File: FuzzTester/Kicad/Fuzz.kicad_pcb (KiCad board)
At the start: 2 copper layers, 180 x 100 mm, 133 parts, among them J1 Audio In/Out JST XH, J10 Key Pad JST XH, J11 1602 LCD JST XH, J2 POT B10K JST XH, J3 POT B5K JST XH, J4 VOL POT A100K JST XH, J5 TestPower_PinHeader, J6 9V Power JST XH, J7 Boot Reset PinHeader, J8 SPI Test PinHeader, J9 SWD_PinHeader, Q1 PN2222A, Q10 2SC1815, Q11 S8050, Q12 S9013, Q13 S9014, Q14 S9018, Q15 BC848B, Q16 2SC1623, Q17 MPSA18, Q18 MPSA18, Q19 2N5088, Q2 MMBT3904, Q20 2N5088, Q21 PN2222A, Q22 MMBT3904, Q23 MMBT5551L, Q24 MMBTA42, Q25 BC807, Q26 BC846, Q27 BC847B, Q28 BC847C, Q29 C945, Q3 MMBT5551L, Q30 2SC1815, Q31 S8050, Q32 S9013, Q33 S9014, Q34 S9018, Q35 BC848B, Q36 2SC1623, Q37 MPSA18, Q38 MPSA18, Q39 2N5088, Q4 MMBTA42, Q40 2N5088, Q5 BC807, Q6 BC846, Q7 BC847B, Q8 BC847C, Q9 C945, U1 AMS1117-5.0, U10 CD4052B, U11 CD4052B, U12 CD4052B, U13 CD4052B, U14 CD4051B, U15 CD4052B, U16 CD4051B, U17 CD4052B, U18 CD4052B, U19 CD4052B, U2 AMS1117-3.3, U20 74HC595, U21 CD4051B, U3 STM32F103C8Tx, U4 CD4051B, U5 74HC595, U6 CD4052B, U7 CD4051B, U8 CD4052B, U9 CD4051B, Y1 8MHz

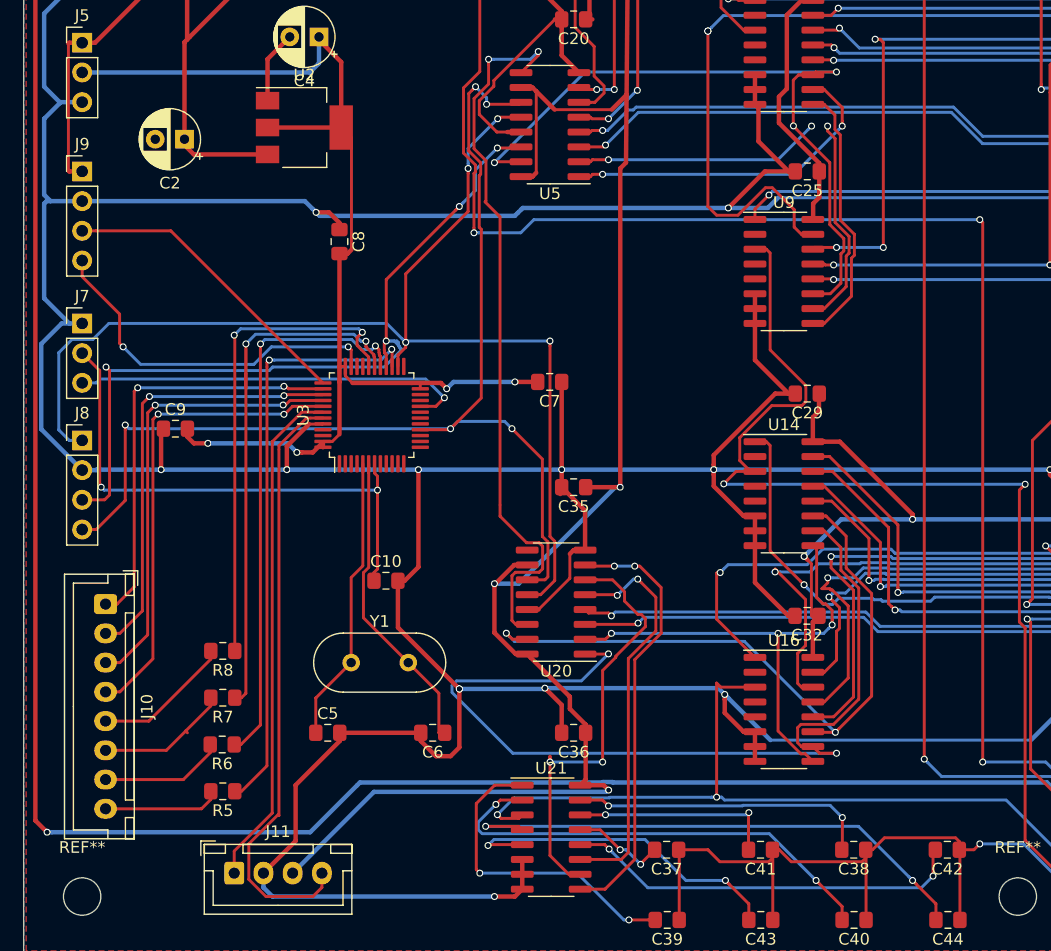
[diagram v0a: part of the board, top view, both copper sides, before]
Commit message: Improved PCB SPI/I2C lines
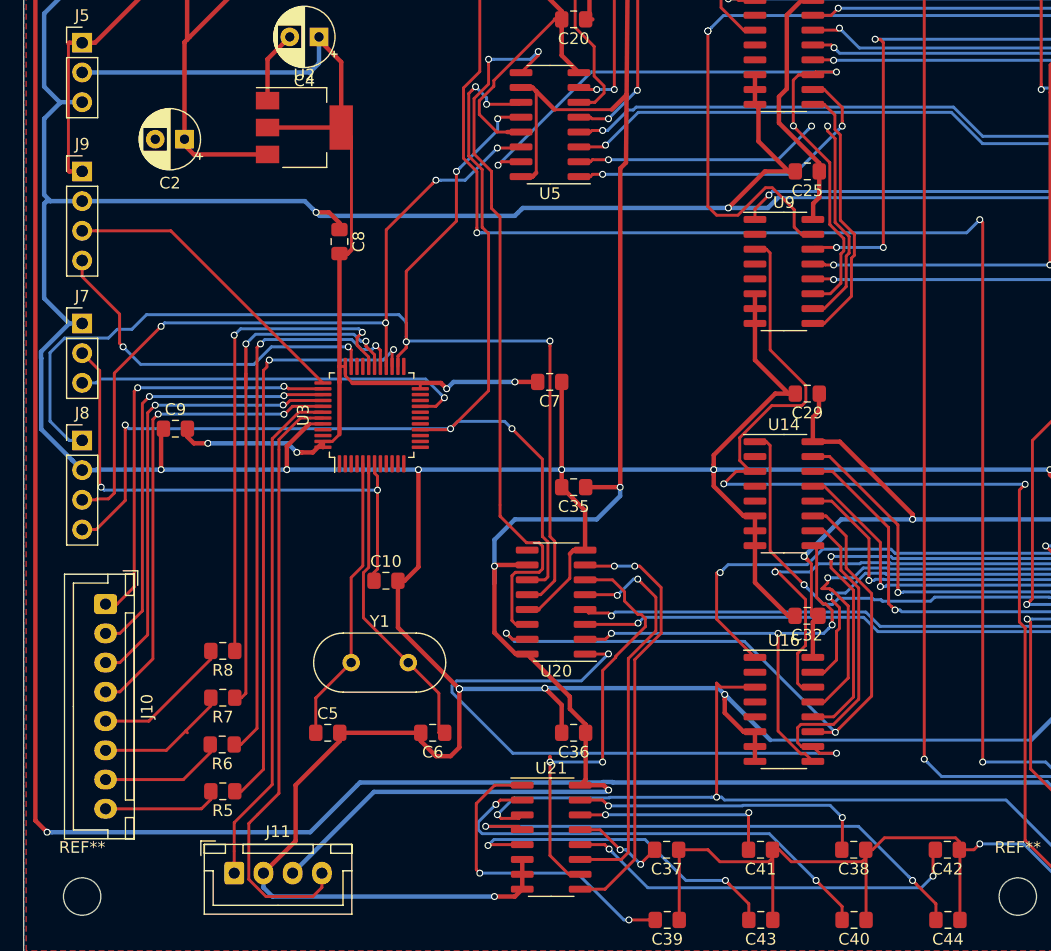
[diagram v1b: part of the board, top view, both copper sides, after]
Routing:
- net /SPI2_MOSI: track 68.0 -> 64.4 mm
- net +5V: track 573.1 -> 576.7 mm
- net /SPI2_CSK: track 103.0 -> 105.6 mm
- net GND: track 1307.9 -> 1307.1 mm

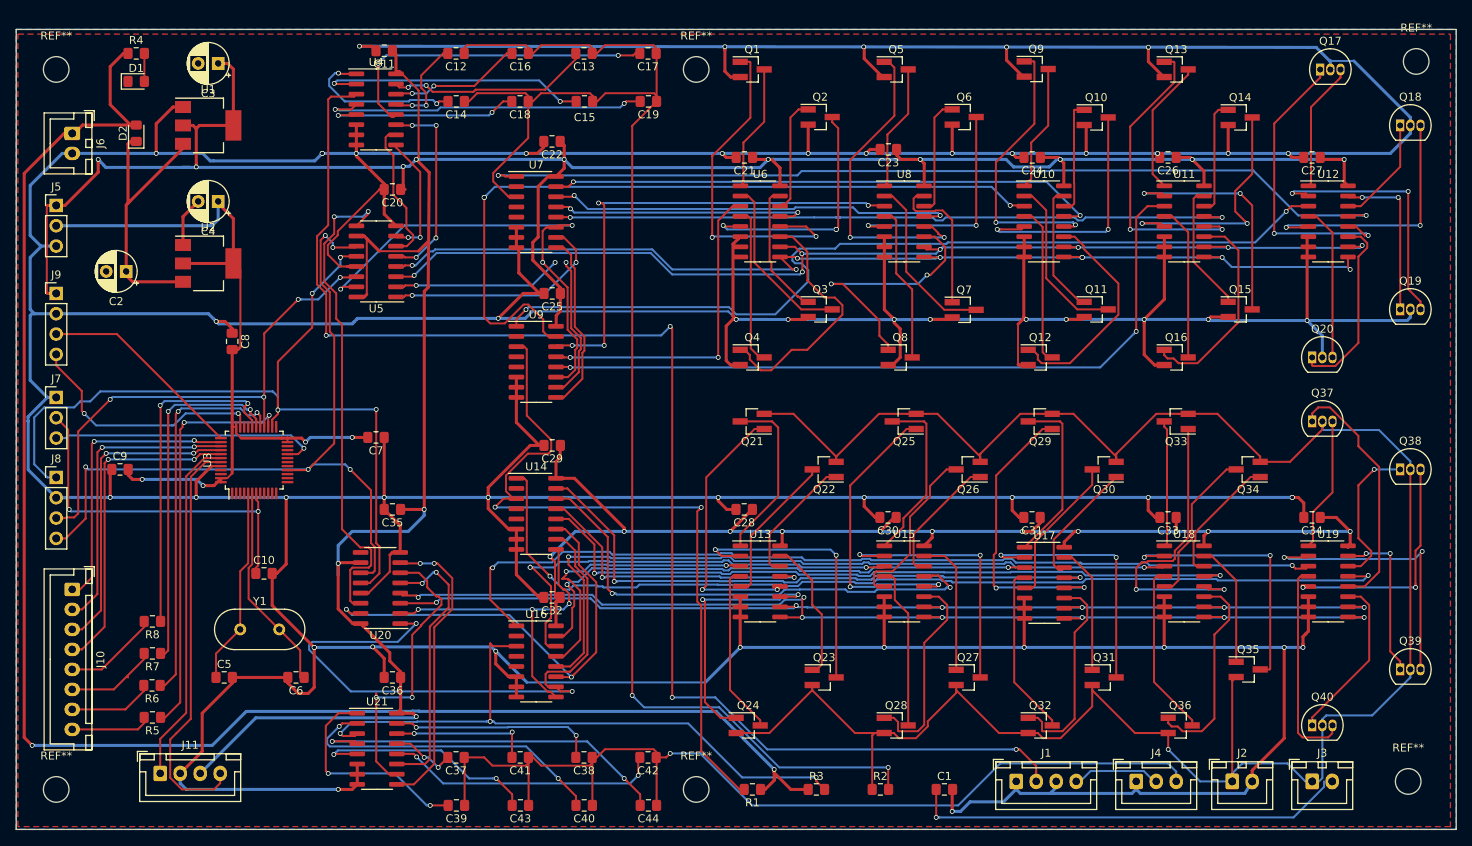
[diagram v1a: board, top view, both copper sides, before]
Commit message: Fixed unconnected PCB traces
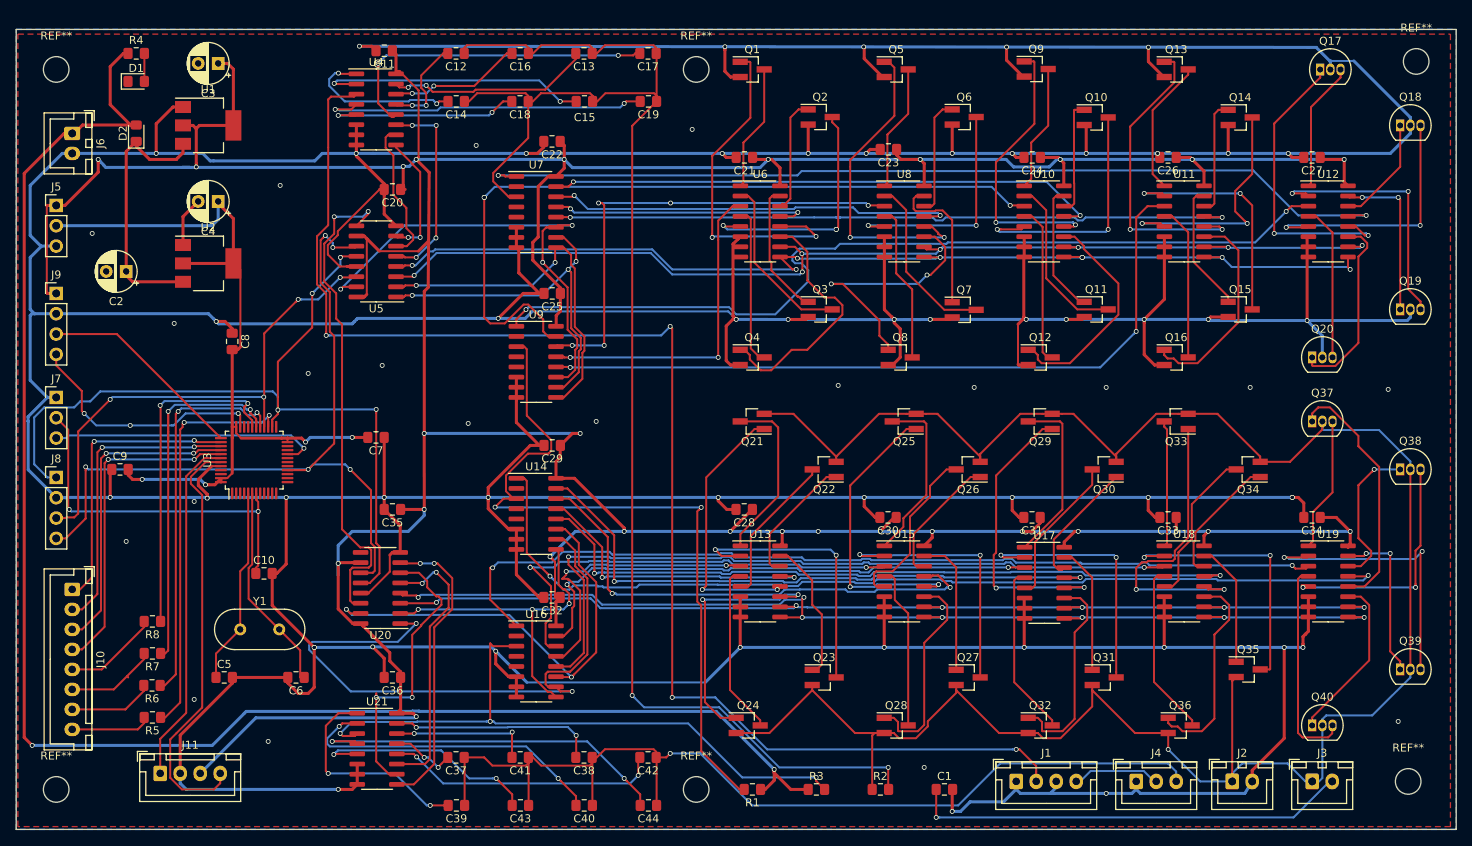
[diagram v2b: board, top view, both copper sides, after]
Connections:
- C2 pad 1: +9V -> Net-(C2-Pad1)
- D2 pad 1: +9V -> Net-(C2-Pad1)
- U1 pad 3: +9V -> Net-(C2-Pad1)
- U2 pad 3: +9V -> Net-(C2-Pad1)
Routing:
- net +9V: track 242.7 -> 207.4 mm
- net Net-(C2-Pad1): track 0.00 -> 33.3 mm
- net +5V: track 576.7 -> 599.9 mm, vias 24 -> 27
- net /TRANSISTOR_B_GROUP_SELECTION_2: track 44.0 -> 45.9 mm
- net /TRANSISTOR_B_GROUP_SELECTION_1: track 47.4 -> 46.2 mm
- net /Mcu/I2C1_SDA: track 51.6 -> 52.8 mm
- net Net-(C1-Pad1): track 54.2 -> 54.9 mm
- net GND: track 1307.1 -> 1307.6 mm, vias 53 -> 72
- net /TransistorsB/TG_2_COLLECTOR: vias 4 -> 5
- net /Mcu/SYS_JTMS_SWDIO: vias 2 -> 3

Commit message: Schematics UI/MCU -> MCU + PCB improvements
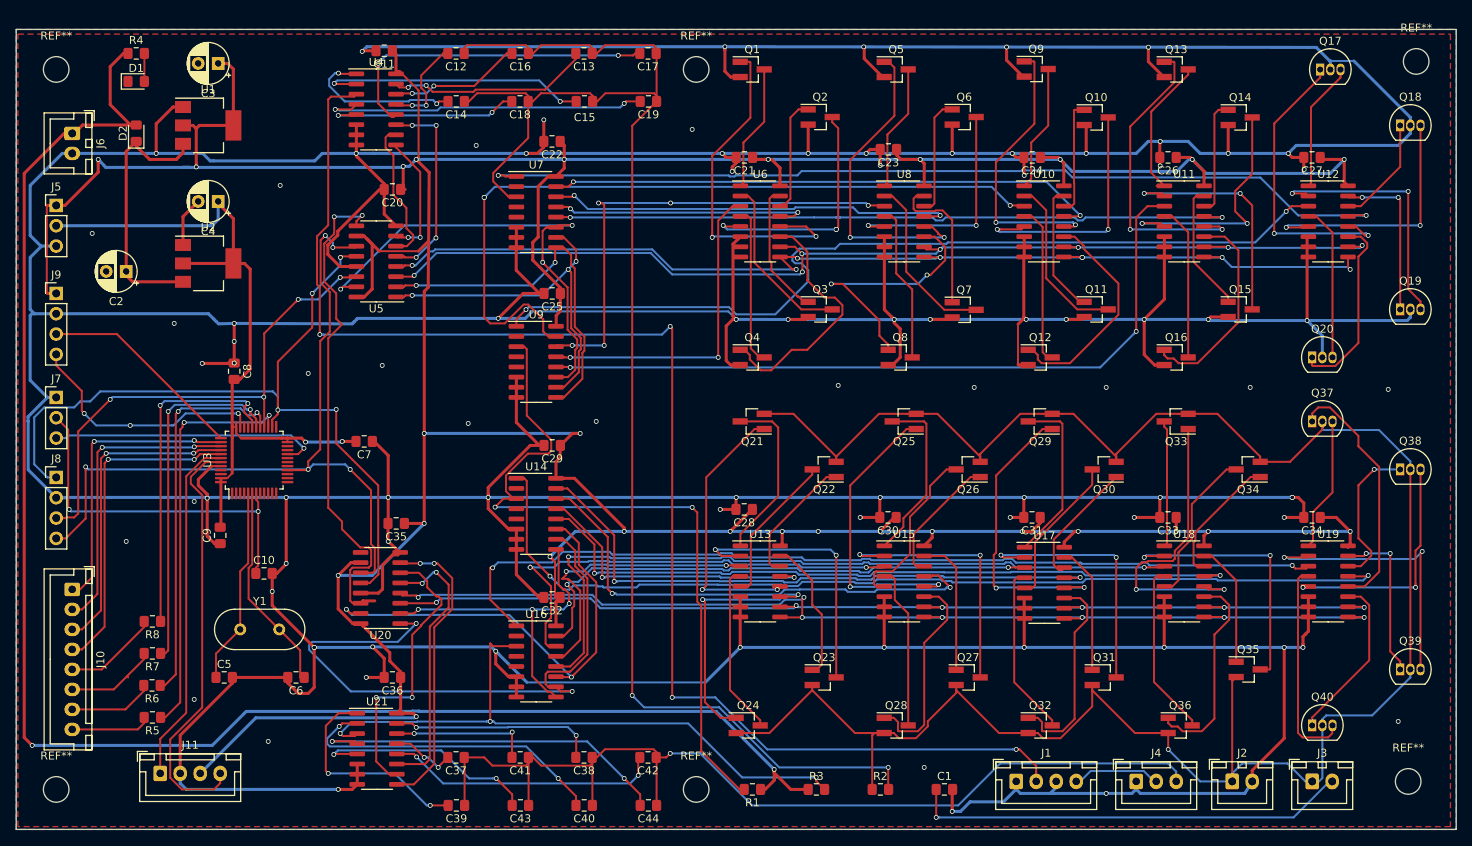
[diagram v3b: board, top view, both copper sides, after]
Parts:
- moved C9 15.0 mm to (54.5, 84.2), turned to 90 degrees
- moved C8 3.73 mm to (56.2, 63.7)
- moved C35 1.81 mm to (76.5, 82.8)
- moved C7 1.56 mm to (72.5, 72.5)
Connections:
- R5 pad 2: Net-(J10-Pad8) -> Net-(R5-Pad2)
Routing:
- net GND: track 1307.6 -> 1339.9 mm, vias 72 -> 89
- net +3V3: track 98.4 -> 92.2 mm, vias 4 -> 2
- net /SPI2_CSK: track 105.6 -> 102.5 mm
- net /ShiftRegistersCD/COMPONENT_SELECTION_INPUT: track 62.1 -> 63.7 mm
- net +5V: track 599.9 -> 598.5 mm
- net /TransistorsB/13_COLLECTOR: track 17.0 -> 18.1 mm
- net /TransistorsC/BASE: track 93.2 -> 92.1 mm
- net /CAPACITOR_D_SELECTION_1: track 37.5 -> 36.5 mm

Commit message: PCB Placement 100x82
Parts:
- removed REF** (x6): MountingHole_3.2mm_M3, MountingHole:MountingHole_3.2mm_M3
- added C45: 100nF, Capacitor_SMD:C_0805_2012Metric_Pad1.15x1.40mm_HandSolder, B.Cu at (63.3, 32.3)
- added C46: 100nF, Capacitor_SMD:C_0805_2012Metric_Pad1.15x1.40mm_HandSolder, B.Cu at (63.0, 98.5)
- added C47: 100nF, Capacitor_SMD:C_0805_2012Metric_Pad1.15x1.40mm_HandSolder, B.Cu at (62.5, 46.0)
- added C48: 100nF, Capacitor_SMD:C_0805_2012Metric_Pad1.15x1.40mm_HandSolder, B.Cu at (63.1, 86.4)
- added H1: MountingHole, MountingHole:MountingHole_3.2mm_M3, F.Cu at (126.5, 33.5)
- added H2: MountingHole, MountingHole:MountingHole_3.2mm_M3, F.Cu at (126.5, 108.5)
- added H3: MountingHole, MountingHole:MountingHole_3.2mm_M3, F.Cu at (33.5, 108.5)
- added H4: MountingHole, MountingHole:MountingHole_3.2mm_M3, F.Cu at (33.5, 33.5)
- added J12: Bypass Switch JST XH, Connector_JST:JST_XH_B2B-XH-A_1x02_P2.50mm_Vertical, F.Cu at (45.2, 99.1)
- added U22: 4504, Package_SO:SOIC-16_3.9x9.9mm_P1.27mm, F.Cu at (61.0, 52.0)
- added U23: 4504, Package_SO:SOIC-16_3.9x9.9mm_P1.27mm, F.Cu at (61.7, 92.9)
- added U24: 4504, Package_SO:SOIC-16_3.9x9.9mm_P1.27mm, F.Cu at (61.8, 105.1)
- added U25: CD4053B, Package_SO:SOIC-16_3.9x9.9mm_P1.27mm, F.Cu at (61.2, 38.5)
- C1: footprint Capacitor_SMD:C_0805_2012Metric_Pad1.15x1.40mm_HandSolder -> Capacitor_THT:CP_Radial_D5.0mm_P2.50mm
- C10, C11, C20, C21, C22, C23, C24, C25, C26, C27, C28, C29, C30, C31, C32, C33, C34, C35, C36, C5, C6, C7, C8, C9: moved to B.Cu
- J11: value 1602 LCD JST XH -> LCD JST XH; footprint Connector_JST:JST_XH_B4B-XH-A_1x04_P2.50mm_Vertical -> Connector_JST:JST_XH_B6B-XH-A_1x06_P2.50mm_Vertical
- J5: value TestPower_PinHeader -> PowerTest_PinHeader; footprint Connector_PinHeader_2.54mm:PinHeader_1x03_P2.54mm_Vertical -> Connector_PinHeader_2.54mm:PinHeader_1x04_P2.54mm_Vertical
- R1, R2, R3: footprint Resistor_SMD:R_0805_2012Metric_Pad1.15x1.40mm_HandSolder -> Resistor_SMD:R_1206_3216Metric_Pad1.42x1.75mm_HandSolder
- moved J3 109.1 mm to (117.3, 34.5)
- moved J2 108.3 mm to (108.5, 34.5)
- moved J4 107.8 mm to (97.2, 34.5)
- moved J1 107.1 mm to (83.3, 34.5)
- moved C1 103.3 mm to (75.0, 40.0)
- moved Q9 103.2 mm to (84.0, 99.4)
- moved R2 102.2 mm to (69.2, 39.6)
- moved Q10 102.0 mm to (84.0, 95.2)
- moved R3 97.3 mm to (76.7, 34.0)
- moved R1 96.8 mm to (69.1, 34.3)
- moved Q6 86.9 mm to (83.9, 91.1)
- moved Q18 83.7 mm to (118.7, 41.5)
- moved Q39 77.5 mm to (125.3, 89.9)
- moved Q5 77.5 mm to (112.3, 98.8)
- moved Q38 76.9 mm to (125.2, 72.4)
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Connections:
- C11 pad 1: +5V -> +9V
- C20 pad 1: +5V -> +3V3
- C21 pad 1: +5V -> +9V
- C22 pad 1: +5V -> +9V
- C23 pad 1: +5V -> +9V
- C24 pad 1: +5V -> +9V
- C25 pad 1: +5V -> +9V
- C26 pad 1: +5V -> +9V
- C27 pad 1: +5V -> +9V
- C28 pad 1: +5V -> +9V
- C29 pad 1: +5V -> +9V
- C30 pad 1: +5V -> +9V
- C31 pad 1: +5V -> +9V
- C32 pad 1: +5V -> +9V
- C33 pad 1: +5V -> +9V
- C34 pad 1: +5V -> +9V
- C35 pad 1: +5V -> +3V3
- C36 pad 1: +5V -> +9V
- J1 pad 2: /JACK_IN_SIGNAL -> /AudioInOut/JACK_IN_SIGNAL
- J1 pad 4: /JACK_OUT_SIGNAL -> /AudioInOut/JACK_OUT_SIGNAL
- J10 pad 1: /Mcu/GPIO_KEYPAD_ROW_1 -> Net-(J10-Pad1)
- J10 pad 2: /Mcu/GPIO_KEYPAD_ROW_2 -> Net-(J10-Pad2)
- J10 pad 3: /Mcu/GPIO_KEYPAD_ROW_3 -> Net-(J10-Pad3)
- J10 pad 4: /Mcu/GPIO_KEYPAD_ROW_4 -> Net-(J10-Pad4)
- J10 pad 5: Net-(J10-Pad5) -> /Mcu/GPIO_KEYPAD_ROW_4
- J10 pad 6: Net-(J10-Pad6) -> /Mcu/GPIO_KEYPAD_ROW_3
- J10 pad 7: Net-(J10-Pad7) -> /Mcu/GPIO_KEYPAD_ROW_2
- J10 pad 8: Net-(J10-Pad8) -> /Mcu/GPIO_KEYPAD_ROW_1
- J4 pad 2: /JACK_OUT_SIGNAL -> /JACK_OUT_SIGNAL_FROM_FUZZ
- J5 pad 1: +5V -> +9V
- J5 pad 2: +3V3 -> +5V
- J5 pad 3: GND -> +3V3
- J6 pad 1: +9V -> GND
- J6 pad 2: GND -> +9V
- R5 pad 1: /Mcu/GPIO_KEYPAD_COLUMN_4 -> /Mcu/GPIO_KEYPAD_COLUMN_1
- R5 pad 2: Net-(R5-Pad2) -> Net-(J10-Pad1)
- R6 pad 1: /Mcu/GPIO_KEYPAD_COLUMN_3 -> /Mcu/GPIO_KEYPAD_COLUMN_2
- R6 pad 2: Net-(J10-Pad7) -> Net-(J10-Pad2)
- R7 pad 1: /Mcu/GPIO_KEYPAD_COLUMN_2 -> /Mcu/GPIO_KEYPAD_COLUMN_3
- R7 pad 2: Net-(J10-Pad6) -> Net-(J10-Pad3)
- R8 pad 1: /Mcu/GPIO_KEYPAD_COLUMN_1 -> /Mcu/GPIO_KEYPAD_COLUMN_4
- R8 pad 2: Net-(J10-Pad5) -> Net-(J10-Pad4)
- U10 pad 16: +5V -> +9V
- U11 pad 16: +5V -> +9V
- U12 pad 16: +5V -> +9V
- U13 pad 16: +5V -> +9V
- U14 pad 16: +5V -> +9V
- U15 pad 16: +5V -> +9V
- U16 pad 16: +5V -> +9V
- U17 pad 16: +5V -> +9V
- U18 pad 16: +5V -> +9V
- U19 pad 16: +5V -> +9V
- U20 pad 1: /TRANSISTOR_C_GROUP_SELECTION_1 -> /TRANSISTOR_C_GROUP_SELECTION_3V3_1
- U20 pad 15: /TRANSISTOR_C_GROUP_SELECTION_0 -> /TRANSISTOR_C_GROUP_SELECTION_3V3_0
- U20 pad 16: +5V -> +3V3
- U20 pad 2: /TRANSISTOR_C_GROUP_SELECTION_2 -> /TRANSISTOR_C_GROUP_SELECTION_3V3_2
- U20 pad 3: /TRANSISTOR_C_SELECTION_0 -> /TRANSISTOR_C_SELECTION_3V3_0
- U20 pad 4: /TRANSISTOR_C_SELECTION_1 -> /TRANSISTOR_C_SELECTION_3V3_1
- U20 pad 5: /CAPACITOR_D_SELECTION_0 -> /CAPACITOR_D_SELECTION_3V3_0
- U20 pad 6: /CAPACITOR_D_SELECTION_1 -> /CAPACITOR_D_SELECTION_3V3_1
- U20 pad 7: /CAPACITOR_D_SELECTION_2 -> /CAPACITOR_D_SELECTION_3V3_2
- U21 pad 16: +5V -> +9V
- U3 pad 12: Net-(U3-Pad12) -> /Mcu/BYPASS_SWITCH_3V3
- U3 pad 13: Net-(U3-Pad13) -> /BYPASS_MODE_3V3
- U4 pad 16: +5V -> +9V
- U4 pad 3: /JACK_IN_SIGNAL -> /JACK_IN_SIGNAL_THROUGH_FUZZ
- U5 pad 1: /TRANSISTOR_B_GROUP_SELECTION_1 -> /TRANSISTOR_B_GROUP_SELECTION_3V3_1
- U5 pad 15: /TRANSISTOR_B_GROUP_SELECTION_0 -> /TRANSISTOR_B_GROUP_SELECTION_3V3_0
- U5 pad 16: +5V -> +3V3
- U5 pad 2: /TRANSISTOR_B_GROUP_SELECTION_2 -> /TRANSISTOR_B_GROUP_SELECTION_3V3_2
- U5 pad 3: /TRANSISTOR_B_SELECTION_0 -> /TRANSISTOR_B_SELECTION_3V3_0
- U5 pad 4: /TRANSISTOR_B_SELECTION_1 -> /TRANSISTOR_B_SELECTION_3V3_1
- U5 pad 5: /CAPACITOR_A_SELECTION_0 -> /CAPACITOR_A_SELECTION_3V3_0
- U5 pad 6: /CAPACITOR_A_SELECTION_1 -> /CAPACITOR_A_SELECTION_3V3_1
- U5 pad 7: /CAPACITOR_A_SELECTION_2 -> /CAPACITOR_A_SELECTION_3V3_2
- U6 pad 16: +5V -> +9V
- U7 pad 16: +5V -> +9V
- U8 pad 16: +5V -> +9V
- U9 pad 16: +5V -> +9V
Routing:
- net GND: track 1339.9 -> 0.00 mm, vias 89 -> 0
- net +5V: track 598.5 -> 35.6 mm, vias 27 -> 0
- net /TransistorsC/EMITTER: track 272.7 -> 0.00 mm, vias 1 -> 0
- net /TransistorsB/BASE: track 191.5 -> 0.00 mm, vias 2 -> 0
- net /JACK_IN_SIGNAL: track 175.6 -> 0.00 mm, vias 4 -> 0
- net +9V: track 207.4 -> 46.7 mm, vias 2 -> 1
- net /TRANSISTOR_B_SELECTION_0: track 138.3 -> 0.00 mm, vias 7 -> 0
- net /TRANSISTOR_C_SELECTION_1: track 136.6 -> 0.00 mm, vias 7 -> 0
- net /TRANSISTOR_B_SELECTION_1: track 135.0 -> 0.00 mm, vias 8 -> 0
- net /TRANSISTOR_C_SELECTION_0: track 132.8 -> 0.00 mm, vias 6 -> 0
- net /TransistorsC/TG_5_BASE: track 121.9 -> 0.00 mm, vias 2 -> 0
- net /TransistorsB/TG_5_BASE: track 115.8 -> 0.00 mm, vias 2 -> 0
- net /TransistorsC/TG_5_COLLECTOR: track 113.5 -> 0.00 mm, vias 2 -> 0
- net /TransistorsB/TG_5_COLLECTOR: track 111.6 -> 0.00 mm, vias 2 -> 0
- net /SPI2_CSK: track 102.5 -> 0.00 mm, vias 4 -> 0
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- removed copper zone on B.Cu, net GND
- removed copper zone on F.Cu, net GND
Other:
- board size 180 x 100 mm -> 100 x 82 mm
- board text added: "1602:BL1 BL2 SDA 5V GND SCL"
- board text added: "5V GND CLK DIO"
- board text added: "9V 5V 3V3 GND"
- board text added: "9V GND"
- board text added: "BP 3V3"
- board text added: "CSK GND MO CSK"
- board text added: "GND IN GND OUT"
- board text added: "GND VOL IN"
- board text added: "IN OUT"
- board text added: "R1 R2 R3 R4 C1 C2 C3 C4"

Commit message: Starting to route
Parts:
- added RN1: R_Pack04, Resistor_SMD:R_Array_Convex_4x0603, F.Cu at (48.6, 58.1)
- added RN2: R_Pack04, Resistor_SMD:R_Array_Convex_4x0603, F.Cu at (37.2, 65.5)
- moved J11 72.9 mm to (55.6, 34.5), turned to 0 degrees
- moved J12 70.8 mm to (74.4, 34.5), turned to 0 degrees
- moved U9 51.5 mm to (60.5, 55.1)
- moved C1 50.2 mm to (125.2, 40.4)
- moved R2 49.9 mm to (119.1, 40.9)
- moved U7 48.7 mm to (71.9, 44.2)
- moved C25 47.8 mm to (66.3, 51.8), turned to 270 degrees
- moved U18 45.5 mm to (71.9, 104.4), turned to 0 degrees
- moved U19 45.2 mm to (83.3, 104.4), turned to 0 degrees
- moved C22 44.9 mm to (77.7, 40.9), turned to 270 degrees
- moved C34 44.2 mm to (89.2, 101.1), turned to 270 degrees
- moved Q5 43.7 mm to (93.7, 59.2)
- moved C33 43.2 mm to (77.7, 101.1), turned to 270 degrees
- moved U11 43.1 mm to (71.9, 66.0), turned to 0 degrees
- moved U12 42.3 mm to (83.3, 66.0), turned to 0 degrees
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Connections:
- U3 pad 16: /GPIO_LATCH -> /Mcu/GPIO_LATCH_MCU
- U3 pad 26: /SPI2_CSK -> /Mcu/SPI2_CSK_MCU
- U3 pad 28: /SPI2_MOSI -> /Mcu/SPI2_MOSI_MCU
- U3 pad 34: /Mcu/SYS_JTMS_SWDIO -> /Mcu/SYS_JTMS_SWDIO_MCU
- U3 pad 37: /Mcu/SYS_JTICK_SWCLK -> /Mcu/SYS_JTICK_SWCLK_MCU
- U3 pad 42: /Mcu/I2C1_SCL -> /Mcu/I2C1_SCL_MCU
- U3 pad 43: /Mcu/I2C1_SDA -> /Mcu/I2C1_SDA_MCU
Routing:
- net /GPIO_LATCH: track 0.00 -> 107.8 mm, vias 0 -> 6
- net /SPI2_CSK: track 0.00 -> 99.9 mm, vias 0 -> 4
- net /Mcu/NRST: track 0.00 -> 73.7 mm, vias 0 -> 2
- net /Mcu/PB2: track 0.00 -> 70.7 mm, vias 0 -> 2
- net /Mcu/BYPASS_SWITCH_3V3: track 0.00 -> 60.6 mm, vias 0 -> 3
- net /Mcu/I2C1_SDA: track 0.00 -> 57.0 mm, vias 0 -> 2
- net /Mcu/I2C1_SCL: track 0.00 -> 48.6 mm, vias 0 -> 2
- net /SPI2_MOSI: track 0.00 -> 47.2 mm, vias 0 -> 3
- net +3V3: track 26.6 -> 72.4 mm, vias 1 -> 4
- net /CapacitorsD/CAPACITOR_AUDIO_OUTPUT: track 43.9 -> 0.00 mm
- net +5V: track 35.6 -> 79.4 mm, vias 0 -> 1
- net /BYPASS_MODE_3V3: track 0.00 -> 39.4 mm, vias 0 -> 2
- net /AudioInOut/JACK_IN_SIGNAL: track 0.00 -> 32.0 mm, vias 0 -> 3
- net +9V: track 46.7 -> 74.1 mm, vias 1 -> 3
- net GND: track 0.00 -> 27.3 mm, vias 0 -> 6
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- added copper zone on B.Cu, net GND
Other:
- board text added: "3V3 BYP"
- board text added: "SCL GND 5V SDA BL1 BL2"
- board text removed: "1602:BL1 BL2 SDA 5V GND SCL"
- board text removed: "BP 3V3"
